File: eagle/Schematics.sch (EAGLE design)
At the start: 56 parts, among them K1 PIN20X2

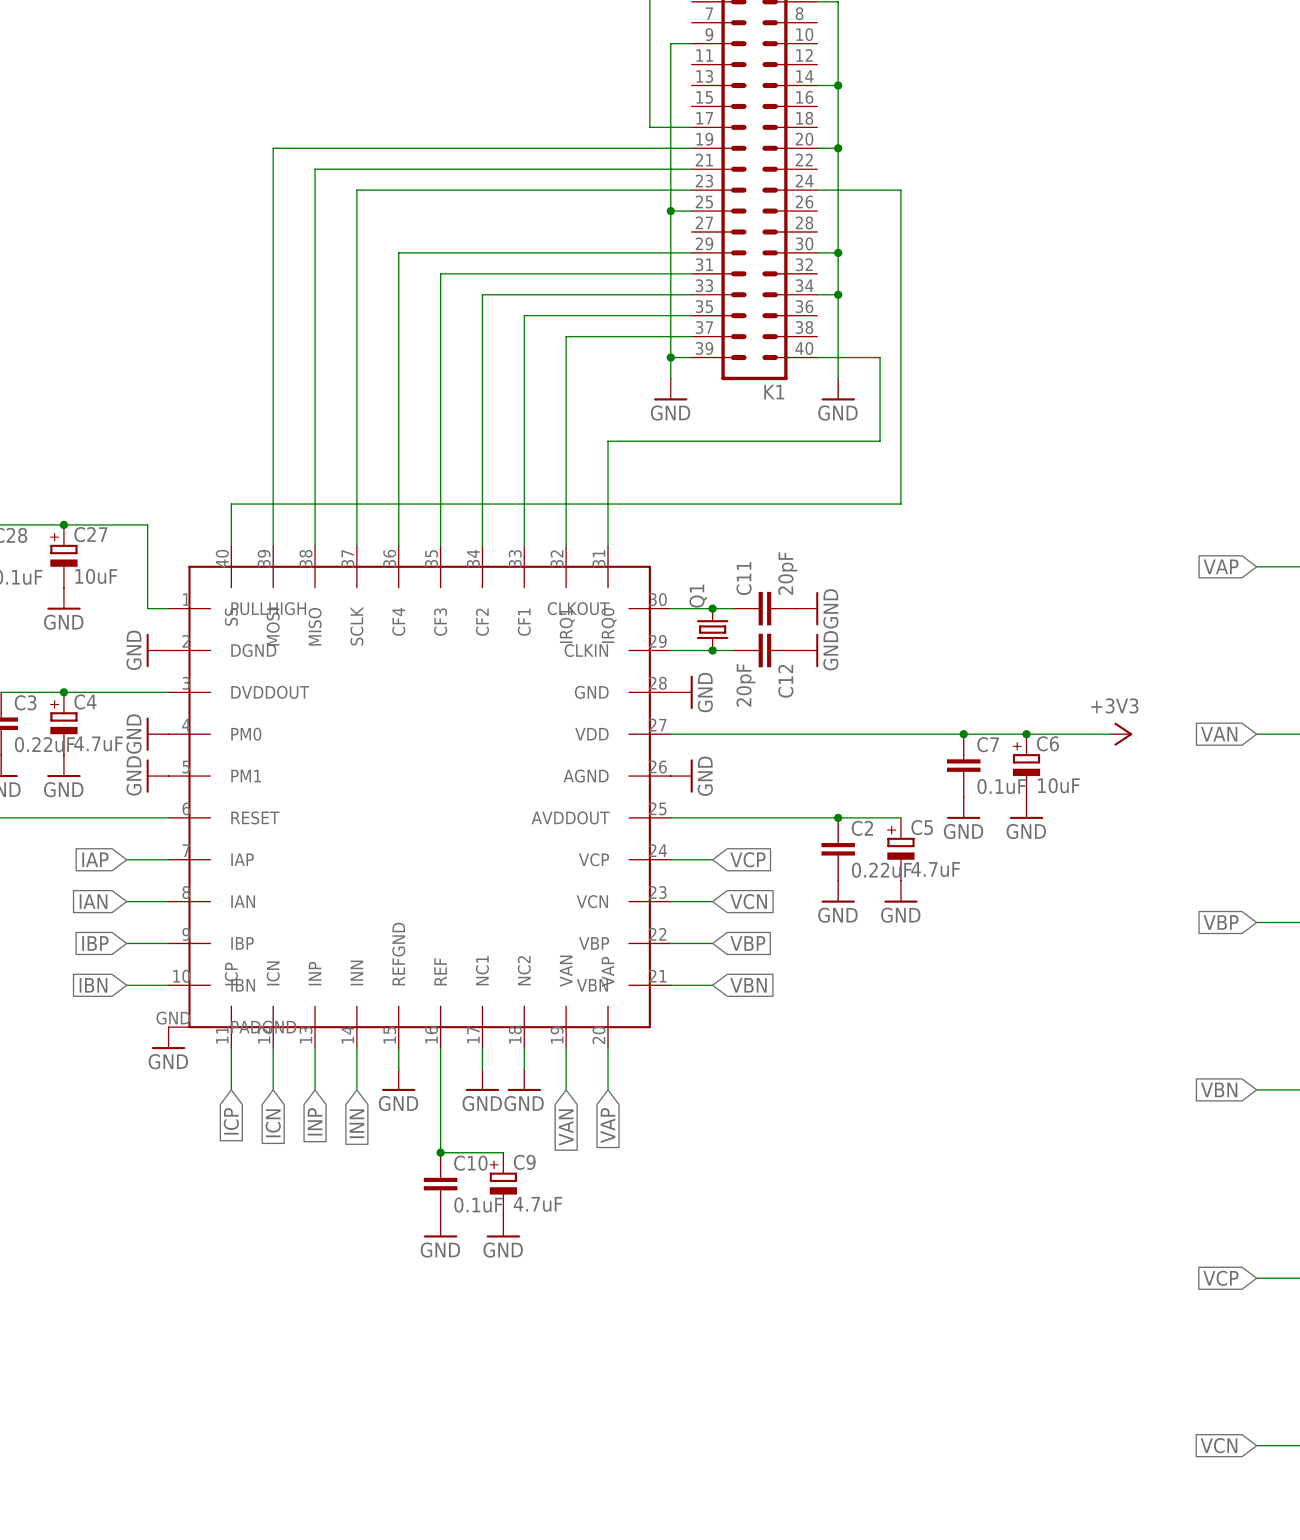
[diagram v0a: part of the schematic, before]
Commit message: fixed symbol; routed GND; rerouted some signals with more space
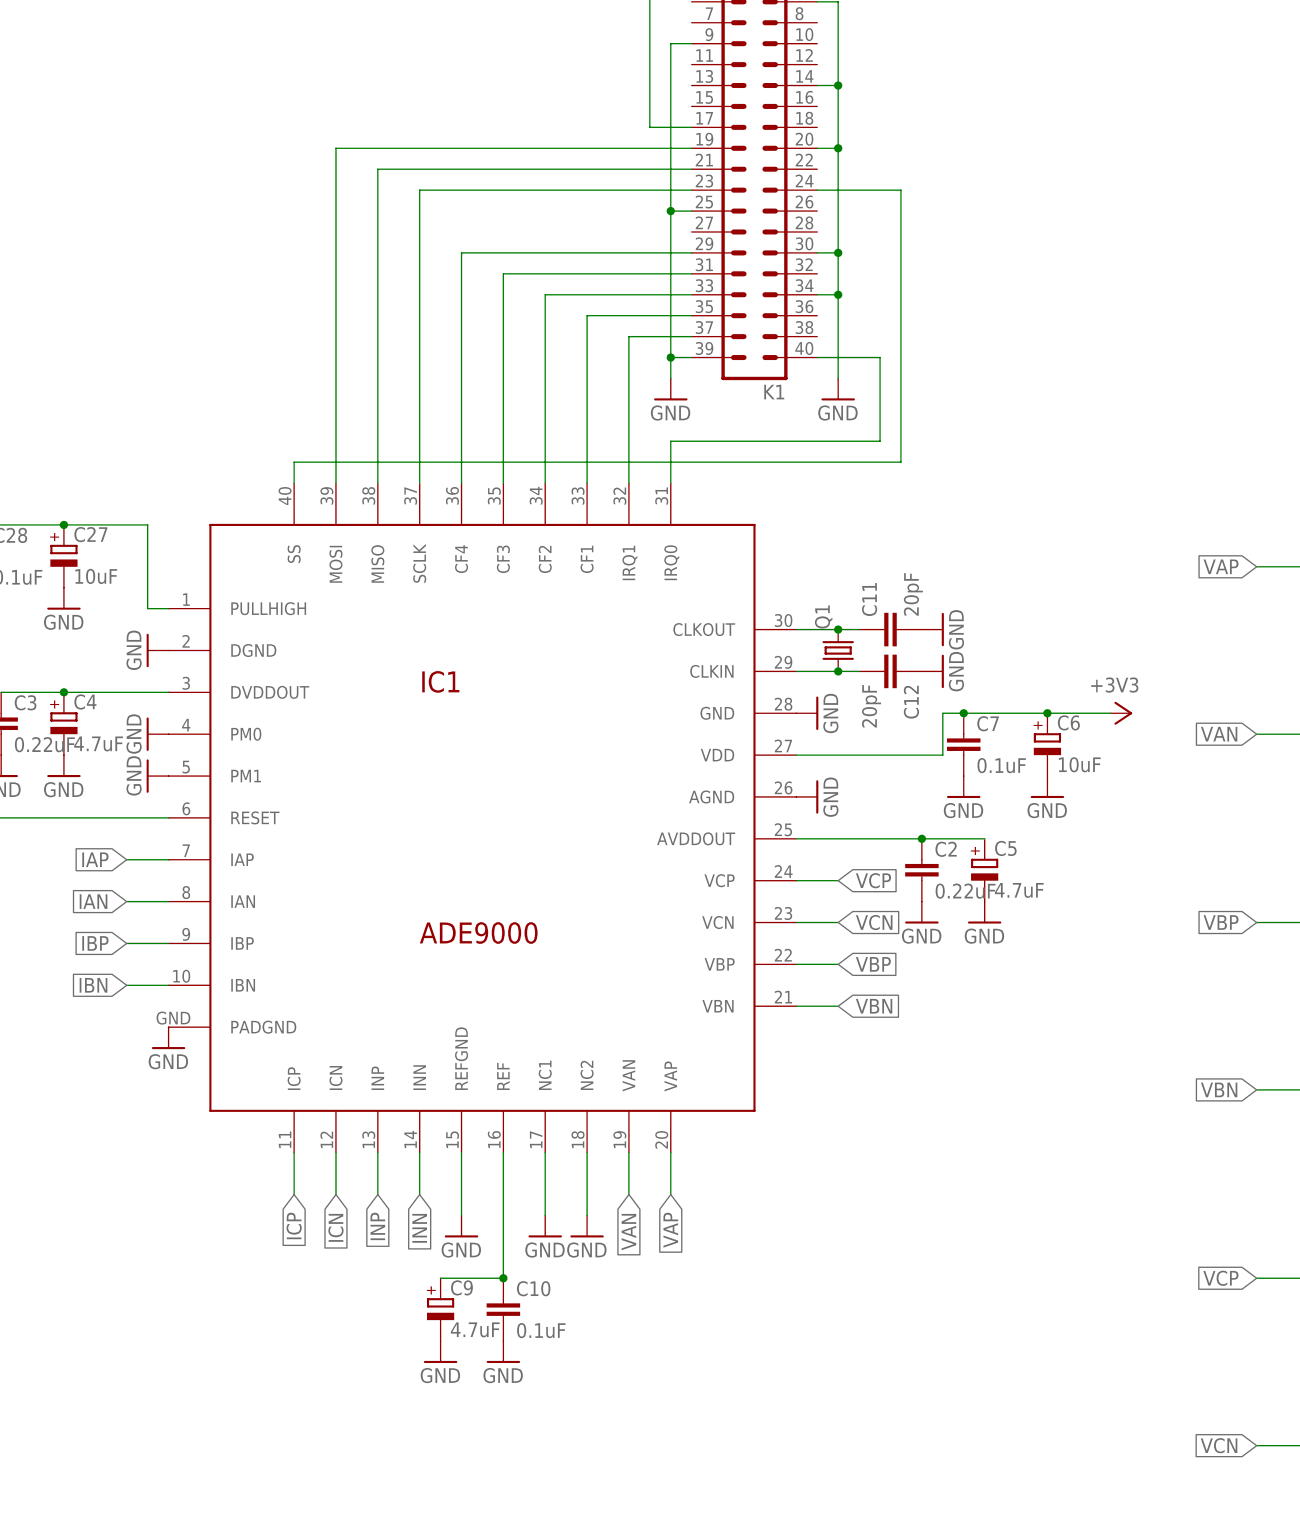
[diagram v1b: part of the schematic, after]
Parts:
- removed $1: ADE9000, ADE9000:ADE9000
- added IC1: ADE9000, ADE9000:ADE9000
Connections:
- net +3V3: now also IC1.PULLHIGH, IC1.VDD; no longer $1.PULLHIGH, $1.VDD
- net GND: now also IC1.AGND, IC1.DGND, IC1.GND, IC1.NC1, IC1.NC2, IC1.PADGND, IC1.PM0, IC1.PM1, IC1.REFGND; no longer $1.AGND, $1.DGND, $1.GND, $1.NC1, $1.NC2, $1.PADGND, $1.PM0, $1.PM1, $1.REFGND
- net IAN: now also IC1.IAN; no longer $1.IAN
- net IAP: now also IC1.IAP; no longer $1.IAP
- net IBN: now also IC1.IBN; no longer $1.IBN
- net IBP: now also IC1.IBP; no longer $1.IBP
- net ICN: now also IC1.ICN; no longer $1.ICN
- net ICP: now also IC1.ICP; no longer $1.ICP
- net INN: now also IC1.INN; no longer $1.INN
- net INP: now also IC1.INP; no longer $1.INP
- net N$1: now also IC1.IRQ1; no longer $1.IRQ1
- net N$2: now also IC1.CF1; no longer $1.CF1
- net N$21: now also IC1.CF3; no longer $1.CF3
- net N$22: now also IC1.CF4; no longer $1.CF4
- net N$23: now also IC1.IRQ0; no longer $1.IRQ0
- net N$24: now also IC1.MOSI; no longer $1.MOSI
- net N$25: now also IC1.MISO; no longer $1.MISO
- net N$26: now also IC1.SCLK; no longer $1.SCLK
- net N$27: now also IC1.SS; no longer $1.SS
- net N$3: now also IC1.CF2; no longer $1.CF2
- net N$4: now also IC1.AVDDOUT; no longer $1.AVDDOUT
- net N$5: now also IC1.DVDDOUT; no longer $1.DVDDOUT
- net N$6: now also IC1.RESET; no longer $1.RESET
- net N$7: now also IC1.REF; no longer $1.REF
- net N$8: now also IC1.CLKOUT; no longer $1.CLKOUT
- net N$9: now also IC1.CLKIN; no longer $1.CLKIN
- net VAN: now also IC1.VAN; no longer $1.VAN
- net VAP: now also IC1.VAP; no longer $1.VAP
- net VBN: now also IC1.VBN; no longer $1.VBN
- net VBP: now also IC1.VBP; no longer $1.VBP
- net VCN: now also IC1.VCN; no longer $1.VCN
- net VCP: now also IC1.VCP; no longer $1.VCP
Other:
- moved on the sheet: C10, C11, C12, C2, C5, C6, C7, C9, Q1

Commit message: Changes
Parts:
- removed C14, C15, C16, C17, C18, C19, C20, C21, C22, C23, C24, C25, C26: 22nF, resistor:C-EUC0805
- removed C27: 10uF, resistor:CPOL-EUC
- removed C28: 0.1uF, resistor:C-EUC0805
- removed IC1: ADE9000, ADE9000:ADE9000
- removed K1: PIN20X2, FLYFISH:PIN20X2
- removed R10, R13, R14, R17, R18, R21, R22, R24, R25, R27, R28, R5, R6, R9: 1k, resistor:R-EU_M0805
- removed R23, R26, R29: 500k, resistor:R-EU_M1206
- removed R4: 10k, resistor:R-EU_M0805
- removed V: (no value), con-wago-500:W237-4
- added ADE9000: ADE9000, ADE9000:ADE9000
- added ADUM4151: ADUM4151, ADUM4151:ADUM4151
- added ADUM6404: ADUM6404, ADUM6404:ADUM6404
- added C1: 1uF, resistor:C-EUC0805
- added C100, C110, C120, C200, C201, C202, C500, C501, C510, C511, C520, C521, C530, C531: 22nF, resistor:C-EUC0805
- added C101, C111, C121: 51pF, resistor:C-EUC0805
- added C30, C32, C40, C42, C50, C52: 0.1uF, resistor:C-EUC0805
- added C31, C33, C41, C43, C51, C53: 10uF, resistor:C-EUC0805
- added IRM05-5: (no value), meanwell_irm_v6:IRM_05/10
- added JP1: (no value), adafruit:PINHD-2X20
- added L: (no value), con-wago-500:W237-4
- added R100, R101, R102, R103, R110, R111, R112, R113, R120, R121, R122, R123: 200k, resistor:R-EU_M1206
- added R104, R114, R124, R200, R201, R202, R500, R501, R510, R511, R520, R521, R530, R531: 1k, resistor:R-EU_M0805
- added U$5: ADP122AUJZ-3.3-R7, ADP122AUJZ-3.3-R7:ADP122AUJZ-3.3-R7
- C11: value 20pF -> 10uF
- C12: value 20pF -> 0.1uF
- C13: value 22nF -> 4.7uF
- C2: value 0.22uF -> 0.1uF
- C3: value 0.22uF -> 4.7uF
- C4: value 4.7uF -> 0.1uF; device resistor:CPOL-EUC -> resistor:C-EUC0805
- C5: device resistor:CPOL-EUC -> resistor:C-EUC0805
- C6: value 10uF -> 0.1uF; device resistor:CPOL-EUC -> resistor:C-EUC0805
- C7: value 0.1uF -> 4.7uF
- C8: value 1uF -> 18pF
- C9: value 4.7uF -> 18pF; device resistor:CPOL-EUC -> resistor:C-EUC0805
- Q1: device crystal:CRYSTALHC49UP -> crystal:CRYSTALCTS406
- R1, R2, R3: value 500k -> 10k; device resistor:R-EU_M1206 -> resistor:R-EU_M0805
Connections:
- removed net +3V3: C27.+, C28.1, C6.+, C7.1, C8.1, IC1.PULLHIGH, IC1.VDD, K1.1, K1.17, R4.2
- removed net N$2: IC1.CF1, K1.35
- removed net N$24: IC1.MOSI, K1.19
- removed net N$25: IC1.MISO, K1.21
- removed net N$26: IC1.SCLK, K1.23
- removed net N$27: IC1.SS, K1.24
- removed net N$5: C3.1, C4.+, IC1.DVDDOUT
- removed net N$6: C8.2, IC1.RESET, R4.1
- removed net N$7: C10.1, C9.+, IC1.REF
- removed net N$8: C11.1, IC1.CLKOUT, Q1.2
- removed net N$9: C12.2, IC1.CLKIN, Q1.1
- new net +3V3_ADE: ADE9000.PM0, ADE9000.PULLHIGH, ADE9000.VDD, ADUM4151.VDD2, C12.1, C13.1, C32.1, C33.1, C52.1, C53.1, R1.2, R3.2, U$5.VOUT
- new net +3V3_ISO: ADUM4151.VDD1, C30.1, C31.1, JP1.1, JP1.17
- new net +5V_ADE: ADUM6404.VISO, ADUM6404.VSEL, C42.1, C43.1, C50.1, C51.1, U$5.EN, U$5.VIN
- new net +5V_ISO: ADUM6404.VDD1, ADUM6404.VDDL, C10.1, C11.1, C40.1, C41.1, IRM05-5.V+, JP1.2, JP1.4
- new net AGND: ADUM4151.GND1, ADUM4151.GND11, ADUM4151.VOC, ADUM6404.GND1, ADUM6404.GND1_1, C10.2, C11.2, C30.2, C31.2, C40.2, C41.2, IRM05-5.V-, JP1.14, JP1.20, JP1.25, JP1.30, JP1.34, JP1.39, JP1.6, JP1.9
- new net AVDDOUT: ADE9000.AVDDOUT, C6.1, C7.1
- new net CF1_ADE: ADE9000.CF1, ADUM6404.VIC
- new net CF1_ISO: ADUM6404.VOC, JP1.31
- new net CF2_ADE: ADE9000.CF2, ADUM6404.VID
- new net CF2_ISO: ADUM6404.VOD, JP1.33
- new net CLKIN: ADE9000.CLKIN, C9.1, Q1.2
- new net CLKOUT: ADE9000.CLKOUT, C8.1, Q1.1
- new net DVDDOUT: ADE9000.DVDDOUT, C2.1, C3.1
- new net IRQ0_ADE: ADE9000.IRQ0, ADUM6404.VIA
- new net IRQ0_ISO: ADUM6404.VOA, JP1.27
- new net IRQ1_ADE: ADE9000.IRQ1, ADUM6404.VIB
- new net IRQ1_ISO: ADUM6404.VOB, JP1.29
- new net MISO_ADE: ADE9000.MISO, ADUM4151.SO
- new net MISO_ISO: ADUM4151.MI, JP1.21
- new net MOSI_ADE: ADE9000.MOSI, ADUM4151.SI
- new net MOSI_ISO: ADUM4151.MO, JP1.19
- new net PM1_ADE: ADE9000.PM1, ADUM4151.VOA, R2.2
- new net PM1_ISO: ADUM4151.VIA, JP1.35
- new net REF: ADE9000.REF, C4.1, C5.1
- new net RESET_ADE: ADE9000.RESET, ADUM4151.VOB, C1.1, R3.1
- new net RESET_ISO: ADUM4151.VIB, JP1.37
- new net SCLK_ADE: ADE9000.SCLK, ADUM4151.SCLK
- new net SCLK_ISO: ADUM4151.MCLK, JP1.23
- new net SS_ADE: ADE9000.SS, ADUM4151.SSS, R1.1
- new net SS_ISO: ADUM4151.MSS, JP1.24
- net GND: now also ADE9000.AGND, ADE9000.CF3, ADE9000.CF4, ADE9000.DGND, ADE9000.GND, ADE9000.NC1, ADE9000.NC2, ADE9000.PADGND, ADE9000.REFGND, ADUM4151.GND2, ADUM4151.GND22, ADUM4151.VIC, ADUM6404.GNDISO, ADUM6404.GND_ISO_1, C1.2, C100.1, C110.1, C12.2, C120.1, C13.2, C200.1, C201.1, C202.1, C32.2, C33.2, C4.2, C42.2, C43.2, C5.2, C50.2, C500.1, C501.2, C51.2, C510.1, C511.2, C52.2, C520.1, C521.2, C53.2, C530.1, C531.2, C6.2, C8.2, C9.2, IRM05-5.AC/N, L-4.KL, R104.2, R114.2, R124.2, R2.1, R200.2, R201.2, R202.2, U$5.GND, U$5.NC; no longer C10.2, C11.2, C12.1, C13.1, C14.2, C15.1, C16.2, C17.1, C18.2, C19.1, C20.2, C21.1, C22.1, C23.1, C24.1, C25.1, C26.1, C27.-, C28.2, C4.-, C5.-, C6.-, C9.-, IC1.AGND, IC1.DGND, IC1.GND, IC1.NC1, IC1.NC2, IC1.PADGND, IC1.PM0, IC1.PM1, IC1.REFGND, K1.14, K1.20, K1.25, K1.30, K1.34, K1.39, K1.6, K1.9, R21.2, R22.2, R24.2, R25.2, R27.2, R28.2, V-4.KL
- net IAN: now also ADE9000.IAN, C501.1, R501.1; no longer C14.1, IC1.IAN, R6.1
- net IAP: now also ADE9000.IAP, C500.2, R500.1; no longer C13.2, IC1.IAP, R5.1
- net IBN: now also ADE9000.IBN, C511.1, R511.1; no longer C16.1, IC1.IBN, R10.1
- net IBP: now also ADE9000.IBP, C510.2, R510.1; no longer C15.2, IC1.IBP, R9.1
- net ICN: now also ADE9000.ICN, C521.1, R521.1; no longer C18.1, IC1.ICN, R14.1
- net ICP: now also ADE9000.ICP, C520.2, R520.1; no longer C17.2, IC1.ICP, R13.1
- net INN: now also ADE9000.INN, C531.1, R531.1; no longer C20.1, IC1.INN, R18.1
- net INP: now also ADE9000.INP, C530.2, R530.1; no longer C19.2, IC1.INP, R17.1
- net N$1: now also R121.2, R122.1; no longer IC1.IRQ1, K1.37
- net N$10: now also R500.2; no longer R5.2
- net N$11: now also R501.2; no longer R6.2
- net N$12: now also R510.2; no longer R9.2
- net N$13: now also R511.2; no longer R10.2
- net N$14: now also R520.2; no longer R13.2
- net N$15: now also R521.2; no longer R14.2
- net N$16: now also R530.2; no longer R17.2
- net N$17: now also R531.2; no longer R18.2
- net N$18: now also R101.2, R102.1; no longer R23.2, V-1.KL
- net N$19: now also R111.2, R112.1; no longer R26.2, V-2.KL
- net N$20: now also R112.2, R113.1; no longer R29.2, V-3.KL
- net N$21: now also R122.2, R123.1; no longer IC1.CF3, K1.31
- net N$22: now also L-2.KL, R113.2; no longer IC1.CF4, K1.29
- net N$23: now also IRM05-5.AC/L, L-3.KL, R123.2; no longer IC1.IRQ0, K1.40
- net N$29: now also R110.2, R111.1; no longer R2.2, R26.1
- net N$3: now also R102.2, R103.1; no longer IC1.CF2, K1.33
- net N$30: now also R100.2, R101.1; no longer R1.2, R23.1
- net N$31: now also R120.2, R121.1; no longer R29.1, R3.2
- net N$4: now also L-1.KL, R103.2; no longer C2.1, C5.+, IC1.AVDDOUT
- net VAN: now also ADE9000.VAN, C101.1, C200.2, R200.1; no longer C21.2, IC1.VAN, R21.1
- net VAP: now also ADE9000.VAP, C100.2, C101.2, R100.1, R104.1; no longer C22.2, IC1.VAP, R1.1, R22.1
- net VBN: now also ADE9000.VBN, C111.1, C201.2, R201.1; no longer C23.2, IC1.VBN, R24.1
- net VBP: now also ADE9000.VBP, C110.2, C111.2, R110.1, R114.1; no longer C24.2, IC1.VBP, R2.1, R25.1
- net VCN: now also ADE9000.VCN, C121.1, C202.2, R202.1; no longer C25.2, IC1.VCN, R27.1
- net VCP: now also ADE9000.VCP, C120.2, C121.2, R120.1, R124.1; no longer C26.2, IC1.VCP, R28.1, R3.1
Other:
- note added: "ADE9000"
- note added: "ADUM4151"
- note added: "ADUM6404"
- moved on the sheet: C10, C11, C12, C13, C2, C3, C7, C8, L1, L2, L3, N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

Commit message: Changes
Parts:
- removed L: (no value), con-wago-500:W237-4
- added R502, R503, R512, R513, R522, R523, R532, R533: 5.1, Schematics:R-EU_M0805
- added X1: MSTBA4, Schematics:MSTBA4
- ADE9000: device ADE9000:ADE9000 -> Schematics:ADE9000
- ADUM4151: device ADUM4151:ADUM4151 -> Schematics:ADUM4151
- ADUM6404: device ADUM6404:ADUM6404 -> Schematics:ADUM6404
- C1, C10, C100, C101, C11, C110, C111, C12, C120, C121, C13, C2, C200, C201, C202, C3, C30, C31, C32, C33, C4, C40, C41, C42, C43, C5, C50, C500, C501, C51, C510, C511, C52, C520, C521, C53, C530, C531, C6, C7, C8, C9: device resistor:C-EUC0805 -> Schematics:C-EUC0805
- IRM05-5: device meanwell_irm_v6:IRM_05/10 -> Schematics:IRM_05/10
- JP1: device adafruit:PINHD-2X20 -> Schematics:PINHD-2X20
- L1, L2, L3, N: device adafruit:STEREOJACK -> Schematics:STEREOJACK
- Q1: device crystal:CRYSTALCTS406 -> Schematics:CRYSTALCTS406
- R1, R104, R114, R124, R2, R200, R201, R202, R3, R500, R501, R510, R511, R520, R521, R530, R531: device resistor:R-EU_M0805 -> Schematics:R-EU_M0805
- R100, R101, R102, R103, R110, R111, R112, R113, R120, R121, R122, R123: device resistor:R-EU_M1206 -> Schematics:R-EU_M1206
- U$5: device ADP122AUJZ-3.3-R7:ADP122AUJZ-3.3-R7 -> Schematics:ADP122AUJZ-3.3-R7
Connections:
- net GND: now also R502.2, R503.1, R512.2, R513.1, R522.2, R523.1, R532.2, R533.1, X1-4.1; no longer L-4.KL
- net N$10: now also R502.1
- net N$11: now also R503.2
- net N$12: now also R512.1
- net N$13: now also R513.2
- net N$14: now also R522.1
- net N$15: now also R523.2
- net N$16: now also R532.1
- net N$17: now also R533.2
- net N$22: now also X1-2.1; no longer L-2.KL
- net N$23: now also X1-3.1; no longer L-3.KL
- net N$4: now also X1-1.1; no longer L-1.KL
